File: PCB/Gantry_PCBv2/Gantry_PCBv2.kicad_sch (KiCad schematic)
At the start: 158 parts, among them J1 Screw_Terminal_01x02, J10 B2B-XH-A_LF__SN_, J11 USB_C_Receptacle_USB2.0_16P, J12 Conn_01x04_Pin, J13 Conn_01x04_Pin, J14 Conn_01x04_Pin, J15 Conn_01x04_Pin, J16 Conn_01x05_Pin, J17 Conn_01x05_Pin, J2 DCJ200-10-A-XX-X_REVA, J3 Conn_01x03_Pin, J4 Conn_01x14, J5 B2B-XH-A_LF__SN_, J6 B2B-XH-A_LF__SN_, J7 B2B-XH-A_LF__SN_, J8 Conn_01x14, J9 Conn_01x10, Q1 NMOS, Q2 SS8050, Q3 SS8050, SW1 SW_0, SW2 SW_EN, SW3 SW_Push_DPDT, SW4 SW_Push_DPDT, U1 ESP32-WROOM-32E, U10 74HC245, U11 74HC245, U12 MCP23017_SO, U2 MP1584, U3 CH340C, U4 TLV75733PDBV, U5 DRV8825_STEPPER_MOTOR_DRIVER_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, U6 DRV8825_STEPPER_MOTOR_DRIVER_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, U7 TB6612FNG H-bridge Motor Driv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, U8 DRV8825_STEPPER_MOTOR_DRIVER_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, U9 DRV8825_STEPPER_MOTOR_DRIVER_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

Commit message: Added Stepper Motor Driver and DPDT switches Footprints
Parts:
- SW3, SW4: footprint Switches:dpdt_sw_2x03_tht -> dpdt_tht:dpdt_sw_2x03_tht
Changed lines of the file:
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@@
 			)
 		)
-		(property "Footprint" "Switches:dpdt_sw_2x03_tht"
+		(property "Footprint" "dpdt_tht:dpdt_sw_2x03_tht"
 			(at 34.29 303.53 0)
 			(effects
@@
 			)
 		)
-		(property "Footprint" "Switches:dpdt_sw_2x03_tht"
+		(property "Footprint" "dpdt_tht:dpdt_sw_2x03_tht"
 			(at 76.2 303.53 0)
 			(effects

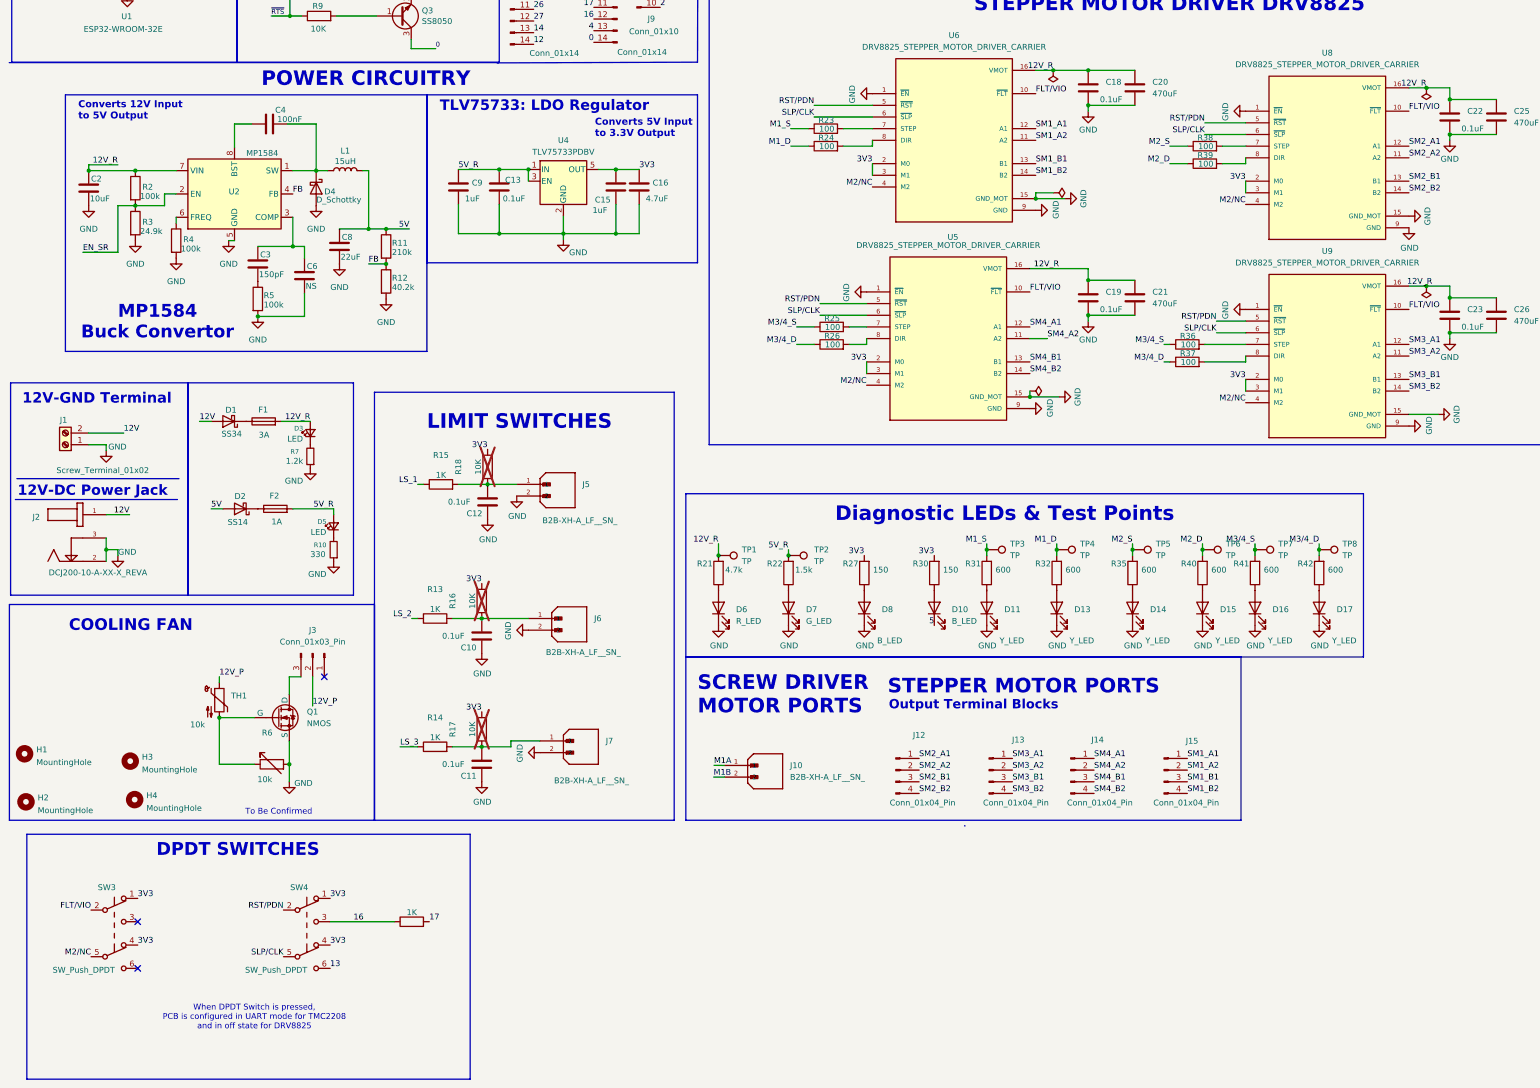
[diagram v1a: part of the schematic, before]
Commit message: fixing errors in schematic
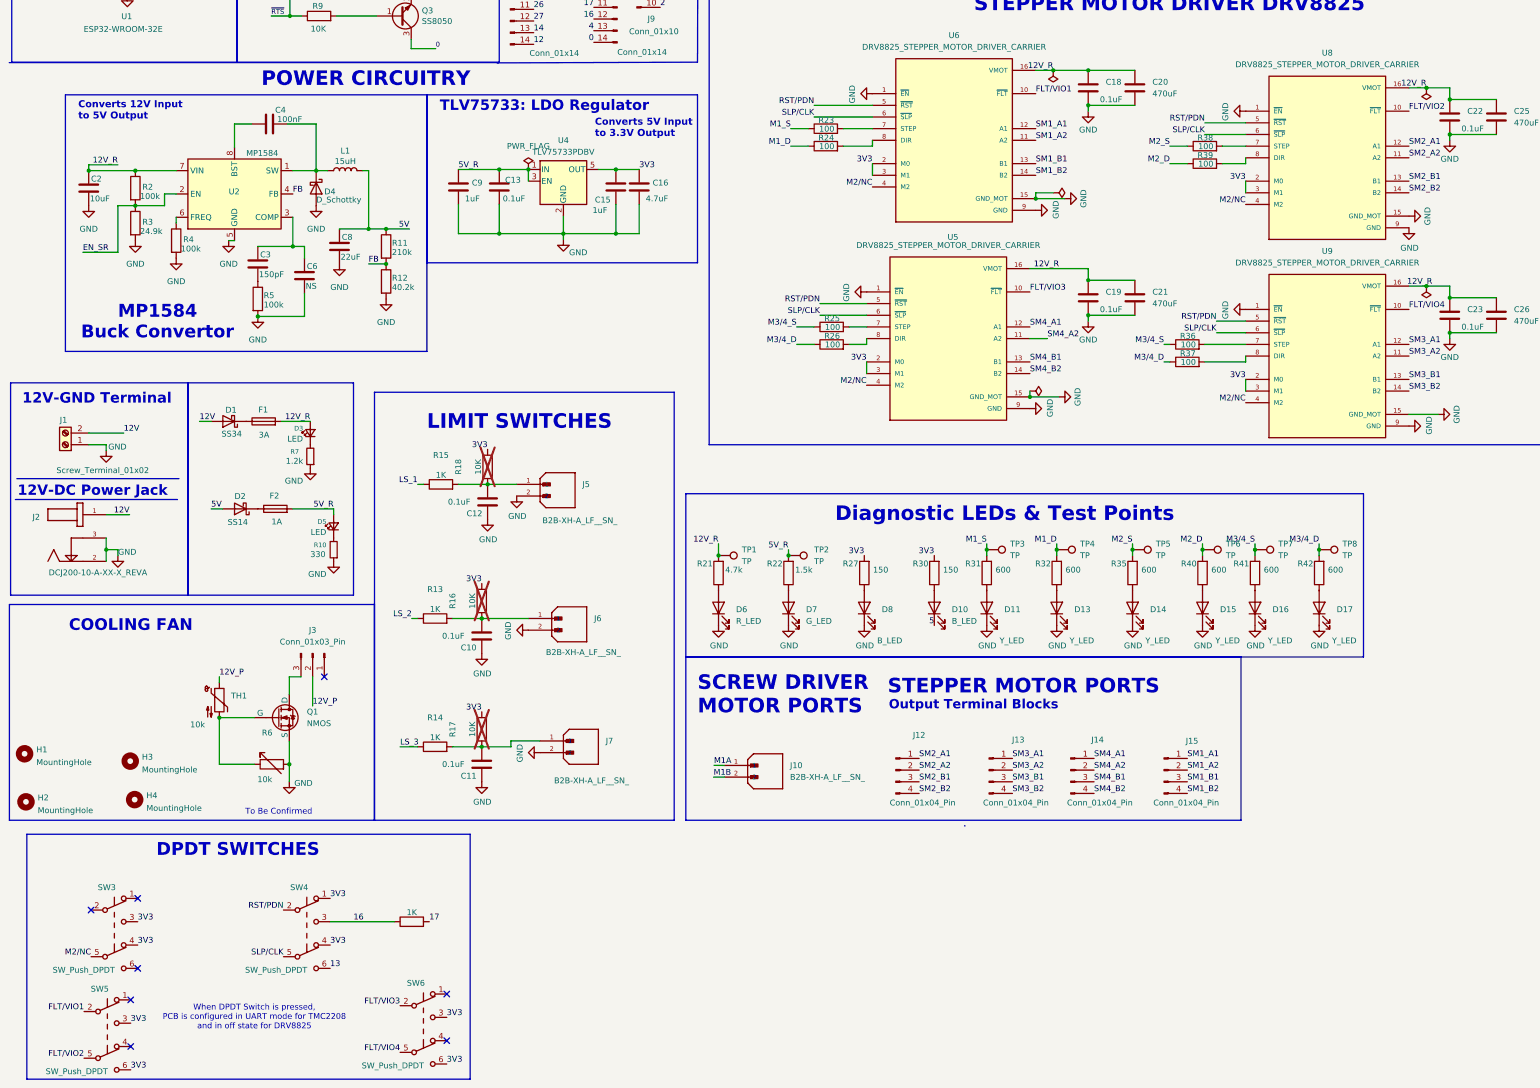
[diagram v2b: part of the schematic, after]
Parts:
- added SW5, SW6: SW_Push_DPDT, dpdt_tht:dpdt_sw_2x03_tht, symbol Switch:SW_Push_DPDT
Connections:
- net 3V3: now also SW3.3 (C), SW5.3 (C), SW5.6 (C), SW6.3 (C), SW6.6 (C); no longer SW3.1 (A)
- removed net FLT/VIO: SW3.2 (B), U5.10 (~{FLT}), U6.10 (~{FLT}), U8.10 (~{FLT}), U9.10 (~{FLT})
- new net FLT/VIO1: SW5.2 (B), U6.10 (~{FLT})
- new net FLT/VIO2: SW5.5 (B), U8.10 (~{FLT})
- new net FLT/VIO3: SW6.2 (B), U5.10 (~{FLT})
- new net FLT/VIO4: SW6.5 (B), U9.10 (~{FLT})
- no-connect marks 36 -> 41
